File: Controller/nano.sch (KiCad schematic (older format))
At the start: 25 parts

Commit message: Almost complete schematic
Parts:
- removed J?: JMP_RESET, OPL_Connector:H2-2.54, symbol Connector:Conn_01x02_Male
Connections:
- net labels added: RST
- wire segments 73 -> 70
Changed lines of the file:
@@
 $Descr A4 11693 8268
 encoding utf-8
-Sheet 3 3
+Sheet 2 4
 Title ""
 Date ""
@@
 	1    0    0    -1
 $EndComp
-$Comp
-L Connector:Conn_01x02_Male J?
-U 1 1 5D4FA25D
-P 7100 1350
-AR Path="/5D499913/5D4FA25D" Ref="J?"  Part="1"
-AR Path="/5D4AF8B7/5D4FA25D" Ref="J?"  Part="1"
-F 0 "J?" H 7072 1232 50  0000 R CNN
-F 1 "JMP_RESET" H 7072 1323 50  0000 R CNN
-F 2 "OPL_Connector:H2-2.54" H 7100 1350 50  0001 C CNN
-F 3 "~" H 7100 1350 50  0001 C CNN
-	1    7100 1350
-	-1   0    0    1
-$EndComp
 Wire Wire Line
 	6700 1400 6800 1400
 Wire Wire Line
-	6900 1400 6900 1350
-Wire Wire Line
 	6800 1400 6800 1750
-Connection ~ 6800 1400
-Wire Wire Line
-	6800 1400 6900 1400
 Connection ~ 6800 2150
-Wire Wire Line
-	6900 1250 6900 1200
-Wire Wire Line
-	6900 1200 6800 1200
 $Comp
 L power:GND #PWR?
@@
 	-1   0    0    1
 $EndComp
-Connection ~ 6800 1200
 Wire Wire Line
 	6800 1200 6700 1200
@@
 Wire Wire Line
 	9400 3150 9750 3150
+Text HLabel 6900 1400 2    50   Input ~ 0
+RST
+Wire Wire Line
+	6900 1400 6800 1400
+Connection ~ 6800 1400
 $EndSCHEMATC

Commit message: Complete schematic
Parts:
- removed J?: USB_B, symbol Connector:USB_B
- added J?: UJ2-BH-1-TH, UJ2-BH-1-TH:CUI_UJ2-BH-1-TH, symbol UJ2-BH-1-TH:UJ2-BH-1-TH
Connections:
- wire segments 70 -> 71
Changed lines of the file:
@@
 L power:GND #PWR?
 U 1 1 5D4AF94B
-P 3400 1850
+P 3700 1750
 AR Path="/5D499913/5D4AF94B" Ref="#PWR?"  Part="1"
 AR Path="/5D4AF8B7/5D4AF94B" Ref="#PWR?"  Part="1"
-F 0 "#PWR?" H 3400 1600 50  0001 C CNN
-F 1 "GND" H 3405 1677 50  0000 C CNN
-F 2 "" H 3400 1850 50  0001 C CNN
-F 3 "" H 3400 1850 50  0001 C CNN
-	1    3400 1850
+F 0 "#PWR?" H 3700 1500 50  0001 C CNN
+F 1 "GND" H 3705 1577 50  0000 C CNN
+F 2 "" H 3700 1750 50  0001 C CNN
+F 3 "" H 3700 1750 50  0001 C CNN
+	1    3700 1750
 	-1   0    0    1
 $EndComp
-$Comp
-L Connector:USB_B J?
-U 1 1 5D4B3A3B
-P 3400 2250
-AR Path="/5D499913/5D4B3A3B" Ref="J?"  Part="1"
-AR Path="/5D4AF8B7/5D4B3A3B" Ref="J?"  Part="1"
-F 0 "J?" H 3170 2147 50  0000 R CNN
-F 1 "USB_B" H 3170 2238 50  0000 R CNN
-F 2 "" H 3550 2200 50  0001 C CNN
-F 3 " ~" H 3550 2200 50  0001 C CNN
-	1    3400 2250
-	1    0    0    1
-$EndComp
 Wire Wire Line
 	3700 2150 4750 2150
 Wire Wire Line
 	4750 2250 3700 2250
-Wire Wire Line
-	3300 1850 3400 1850
-Connection ~ 3400 1850
-NoConn ~ 3700 2450
 NoConn ~ 5550 1650
 NoConn ~ 4750 1750
@@
 	6900 1400 6800 1400
 Connection ~ 6800 1400
+$Comp
+L UJ2-BH-1-TH:UJ2-BH-1-TH J?
+U 1 1 5D55598E
+P 3300 2150
+F 0 "J?" H 3407 2617 50  0000 C CNN
+F 1 "UJ2-BH-1-TH" H 3407 2526 50  0000 C CNN
+F 2 "UJ2-BH-1-TH:CUI_UJ2-BH-1-TH" H 3300 2150 50  0001 L BNN
+F 3 "" H 3300 2150 50  0001 L BNN
+F 4 "UJ2-BH-1-TH" H 3300 2150 50  0001 C CNN "MPN"
+F 5 "102-3999-ND" H 3300 2150 50  0001 C CNN "DK_PN"
+F 6 "https://www.digikey.com/product-detail/en/cui-inc/UJ2-BH-1-TH/102-3999-ND/6187914" H 3300 2150 50  0001 C CNN "DigiKey Product"
+F 7 "https://www.cui.com/product/resource/digikeypdf/uj2-bh-th.pdf" H 3300 2150 50  0001 C CNN "Datasheet"
+	1    3300 2150
+	1    0    0    1
+$EndComp
+Wire Wire Line
+	3700 1750 3700 1850
+Wire Wire Line
+	3700 1850 3700 2050
+Connection ~ 3700 1850
+NoConn ~ 3700 2350
 $EndSCHEMATC

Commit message: Set more footprints
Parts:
- J10: renamed from J?; footprint (none) -> Connector_PinHeader_2.54mm:PinHeader_2x03_P2.54mm_Vertical; MPN (none) -> P125-12A1BS116A1; SKU (none) -> 320020077
- gave numbers to parts that had none: 23

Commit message: Add IC footprints
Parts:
- U2: footprint (none) -> OPL_Integrated_Circuit:SSOP20-0.65-7.6X5.2MM
- U3: footprint (none) -> OPL_Integrated_Circuit:TQFP32-0.8-7X7MM
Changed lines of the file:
@@
 F 0 "U3" H 8450 4704 45  0000 C CNN
 F 1 "MCU-ATMEGA328P-AU_TQFP32_" H 8450 4620 45  0000 C CNN
-F 2 "" H 8450 3300 50  0001 C CNN
+F 2 "OPL_Integrated_Circuit:TQFP32-0.8-7X7MM" H 8450 3300 50  0001 C CNN
 F 3 "" H 8450 3300 50  0001 C CNN
 F 4 "ATMEGA328P-AU" H 8480 3450 20  0001 C CNN "MPN"
@@
 F 0 "U2" H 5150 2754 45  0000 C CNN
 F 1 "INTERFACE-CH340T_SSOP20_" H 5150 2670 45  0000 C CNN
-F 2 "" H 5150 2100 50  0001 C CNN
+F 2 "OPL_Integrated_Circuit:SSOP20-0.65-7.6X5.2MM" H 5150 2100 50  0001 C CNN
 F 3 "" H 5150 2100 50  0001 C CNN
 F 4 "CH340T" H 5180 2250 20  0001 C CNN "MPN"

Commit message: Creating Pi layout
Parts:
- C9: symbol OPL_Capacitor:TANTALUM-SMD-10UF-10V-10%_AVX-A_ -> tantalum-smd-10uf-10v-10%_avx-a_:TANTALUM-SMD-10UF-10V-10%_AVX-A_
- J15: renamed from J9; footprint UJ2-BH-1-TH:CUI_UJ2-BH-1-TH -> CUI:CUI_UJ2-BH-1-TH
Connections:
- net 5V: now also C9.1 (+); no longer C9.+
- net GND: now also C9.2 (-); no longer C9.-
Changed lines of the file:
@@
 $EndComp
 $Comp
-L OPL_Capacitor:TANTALUM-SMD-10UF-10V-10%_AVX-A_ C9
+L tantalum-smd-10uf-10v-10%_avx-a_:TANTALUM-SMD-10UF-10V-10%_AVX-A_ C9
 U 1 1 5D4E7480
 P 6750 3800
@@
 Connection ~ 6800 1400
 $Comp
-L UJ2-BH-1-TH:UJ2-BH-1-TH J9
+L UJ2-BH-1-TH:UJ2-BH-1-TH J15
 U 1 1 5D55598E
 P 3300 2150
-F 0 "J9" H 3407 2617 50  0000 C CNN
+F 0 "J15" H 3407 2617 50  0000 C CNN
 F 1 "UJ2-BH-1-TH" H 3407 2526 50  0000 C CNN
-F 2 "UJ2-BH-1-TH:CUI_UJ2-BH-1-TH" H 3300 2150 50  0001 L BNN
+F 2 "CUI:CUI_UJ2-BH-1-TH" H 3300 2150 50  0001 L BNN
 F 3 "" H 3300 2150 50  0001 L BNN
 F 4 "UJ2-BH-1-TH" H 3300 2150 50  0001 C CNN "MPN"

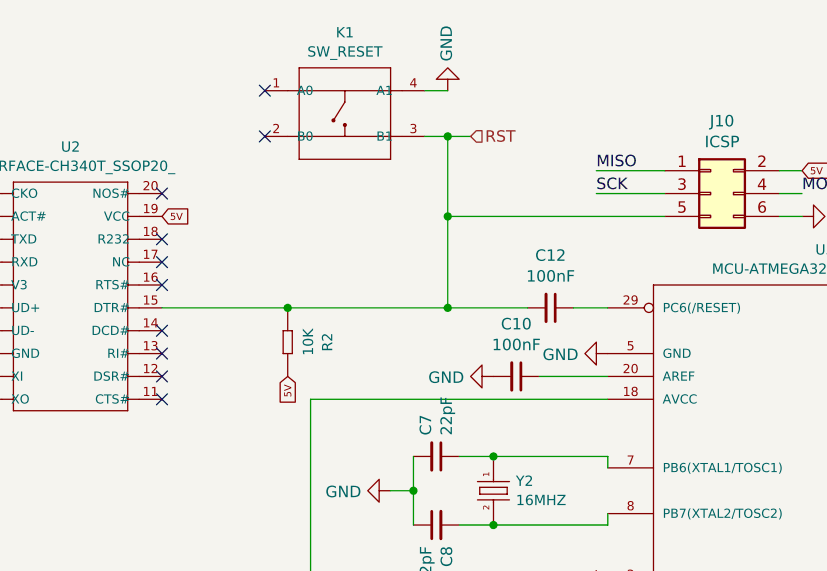
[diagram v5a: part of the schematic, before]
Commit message: power and nano cleanup
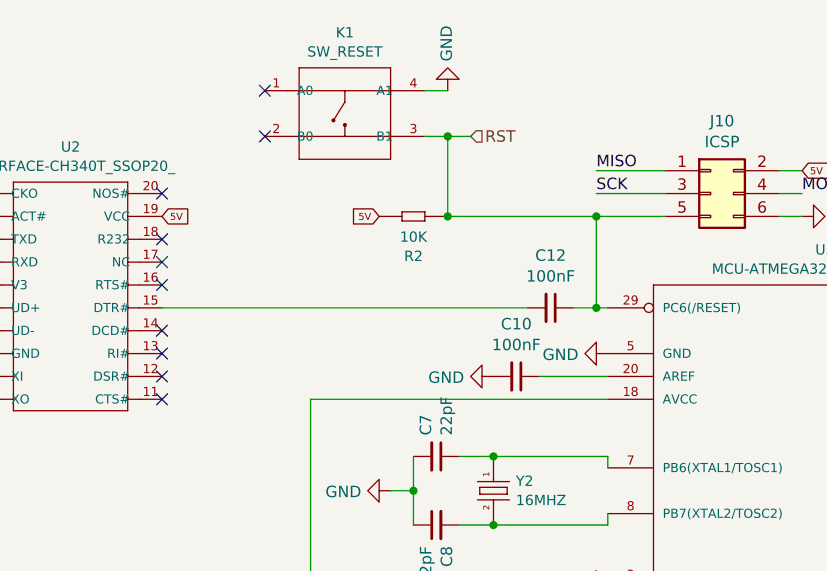
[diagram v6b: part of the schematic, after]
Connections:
- net RST: now also C12.1, U3.29 (PC6(/RESET)); no longer C12.2, U2.15 (DTR#)
- new net: C12.2, U2.15 (DTR#)
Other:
- moved on the sheet: R2
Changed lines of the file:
@@
 	10050 3150 10100 3150
 Wire Wire Line
-	7350 2150 7500 2150
-Wire Wire Line
-	7150 2150 6800 2150
+	7350 2150 7450 2150
 NoConn ~ 5550 1950
 NoConn ~ 5550 2050
@@
 	1    0    0    -1
 $EndComp
-Wire Wire Line
-	6700 1400 6800 1400
-Wire Wire Line
-	6800 1400 6800 1750
-Connection ~ 6800 2150
 $Comp
 L power:GND #PWR018
@@
 Text Label 9750 4400 0    50   ~ 0
 SCK
-Text GLabel 6100 2450 3    31   Input ~ 0
+Text GLabel 6500 1750 0    31   Input ~ 0
 5V
 $Comp
 L OPL_Resistor:SMD-RES-1K-1%-1_10W_0603_ R2
 U 1 1 5D50C710
-P 6100 2300
+P 6650 1750
 AR Path="/5D499913/5D50C710" Ref="R2"  Part="1"
 AR Path="/5D4AF8B7/5D50C710" Ref="R?"  Part="1"
-F 0 "R2" H 6100 2474 45  0000 C CNN
-F 1 "10K" H 6100 2390 45  0000 C CNN
-F 2 "OPL_Resistor:R0603" H 6100 2300 40  0001 C CNN
-F 3 "" H 6100 2300 40  0001 C CNN
-F 4 "RC0603FR-0710KL" H 6130 2450 20  0001 C CNN "MPN"
-F 5 "301010299" H 6130 2450 20  0001 C CNN "SKU"
-	1    6100 2300
-	0    1    1    0
-$EndComp
-Connection ~ 6100 2150
-Wire Wire Line
-	6100 2150 5550 2150
-Wire Wire Line
-	6800 2150 6100 2150
-Wire Wire Line
-	7750 1750 6800 1750
-Connection ~ 6800 1750
-Wire Wire Line
-	6800 1750 6800 2150
+F 0 "R2" H 6650 1924 45  0000 C CNN
+F 1 "10K" H 6650 1840 45  0000 C CNN
+F 2 "OPL_Resistor:R0603" H 6650 1750 40  0001 C CNN
+F 3 "" H 6650 1750 40  0001 C CNN
+F 4 "RC0603FR-0710KL" H 6680 1900 20  0001 C CNN "MPN"
+F 5 "301010299" H 6680 1900 20  0001 C CNN "SKU"
+	1    6650 1750
+	-1   0    0    1
+$EndComp
 Text Label 9750 4200 0    50   ~ 0
 MOSI
@@
 Text HLabel 6900 1400 2    50   Input ~ 0
 RST
-Wire Wire Line
-	6900 1400 6800 1400
-Connection ~ 6800 1400
 $Comp
 L UJ2-BH-1-TH:UJ2-BH-1-TH J15
@@
 Connection ~ 3700 1850
 NoConn ~ 3700 2350
+Wire Wire Line
+	7750 1750 7450 1750
+Wire Wire Line
+	7450 1750 7450 2150
+Connection ~ 7450 2150
+Wire Wire Line
+	7450 2150 7500 2150
+Wire Wire Line
+	6700 1400 6800 1400
+Wire Wire Line
+	6800 1400 6800 1750
+Wire Wire Line
+	6800 1750 7450 1750
+Connection ~ 6800 1400
+Wire Wire Line
+	6800 1400 6900 1400
+Connection ~ 7450 1750
+Connection ~ 6800 1750
+Wire Wire Line
+	5550 2150 7150 2150
 $EndSCHEMATC

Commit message: Mostly final layout
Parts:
- renumbered J15 to J9
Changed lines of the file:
@@
 RST
 $Comp
-L UJ2-BH-1-TH:UJ2-BH-1-TH J15
+L UJ2-BH-1-TH:UJ2-BH-1-TH J9
 U 1 1 5D55598E
 P 3300 2150
-F 0 "J15" H 3407 2617 50  0000 C CNN
+F 0 "J9" H 3407 2617 50  0000 C CNN
 F 1 "UJ2-BH-1-TH" H 3407 2526 50  0000 C CNN
 F 2 "CUI:CUI_UJ2-BH-1-TH" H 3300 2150 50  0001 L BNN

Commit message: Fixing 10uF caps
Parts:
- C9: footprint Capacitor_Tantalum_SMD:CP_EIA-3216-18_Kemet-A -> OPL_Capacitor:C1206; symbol tantalum-smd-10uf-10v-10%_avx-a_:TANTALUM-SMD-10UF-10V-10%_AVX-A_ -> Device:C; MPN TAJA106K010RNJ -> CC1206KKX5R8BB106; SKU 302020011 -> 302010181
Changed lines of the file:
@@
 $EndComp
 $Comp
-L tantalum-smd-10uf-10v-10%_avx-a_:TANTALUM-SMD-10UF-10V-10%_AVX-A_ C9
+L Device:C C9
 U 1 1 5D4E7480
 P 6750 3800
 AR Path="/5D499913/5D4E7480" Ref="C9"  Part="1"
 AR Path="/5D4AF8B7/5D4E7480" Ref="C?"  Part="1"
-F 0 "C9" V 6708 3928 45  0000 L CNN
-F 1 "10uF" V 6792 3928 45  0000 L CNN
-F 2 "Capacitor_Tantalum_SMD:CP_EIA-3216-18_Kemet-A" H 6750 3800 50  0001 C CNN
+F 0 "C9" H 6850 3750 45  0000 L CNN
+F 1 "10uF" H 6850 3850 45  0000 L CNN
+F 2 "OPL_Capacitor:C1206" H 6750 3800 50  0001 C CNN
 F 3 "" H 6750 3800 50  0001 C CNN
-F 4 "TAJA106K010RNJ" H 6780 3950 20  0001 C CNN "MPN"
-F 5 "302020011" H 6780 3950 20  0001 C CNN "SKU"
+F 4 "CC1206KKX5R8BB106" H 6780 3950 20  0001 C CNN "MPN"
+F 5 "302010181" H 6780 3950 20  0001 C CNN "SKU"
 	1    6750 3800
-	0    1    1    0
+	1    0    0    -1
 $EndComp
 Wire Wire Line
 	6300 3700 6300 3650
-Wire Wire Line
-	6300 3650 6750 3650
-Wire Wire Line
-	6750 3650 7150 3650
-Connection ~ 6750 3650
 Wire Wire Line
 	7150 3700 7150 3650
@@
 Wire Wire Line
 	5550 2150 7150 2150
+Wire Wire Line
+	6300 3650 6750 3650
+Connection ~ 6750 3650
+Wire Wire Line
+	6750 3650 7150 3650
 $EndSCHEMATC
